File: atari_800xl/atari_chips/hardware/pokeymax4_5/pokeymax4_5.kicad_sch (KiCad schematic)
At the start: 0 parts

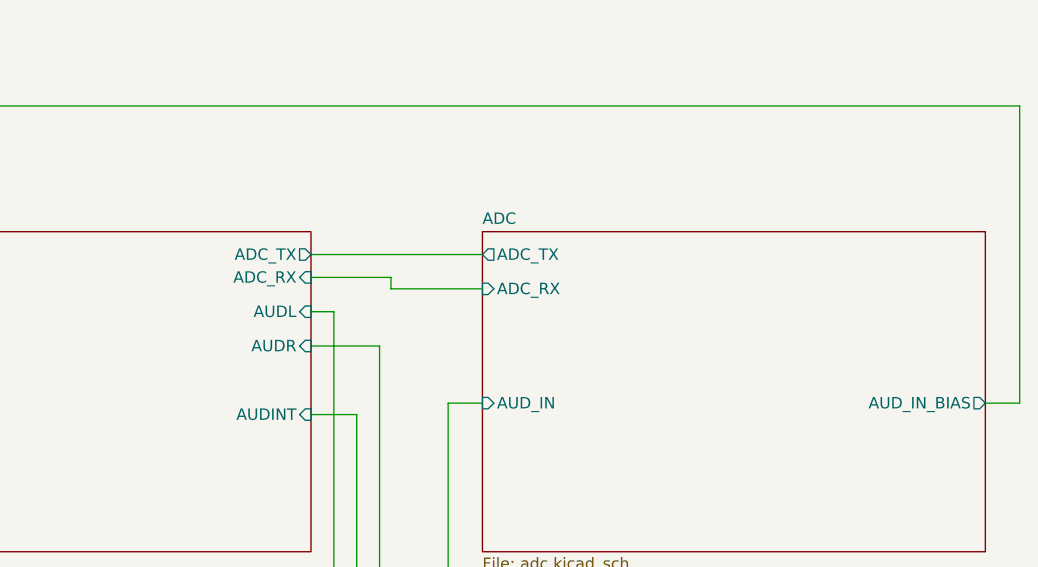
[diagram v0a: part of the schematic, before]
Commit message: Pokeymax v4_53 as produced
git-svn-id: svn+ssh://192.168.0.3/home/svnfpga/repo/trunk@1512 d6161ac3-aae1-4d52-9b05-ea9ac36b53d3
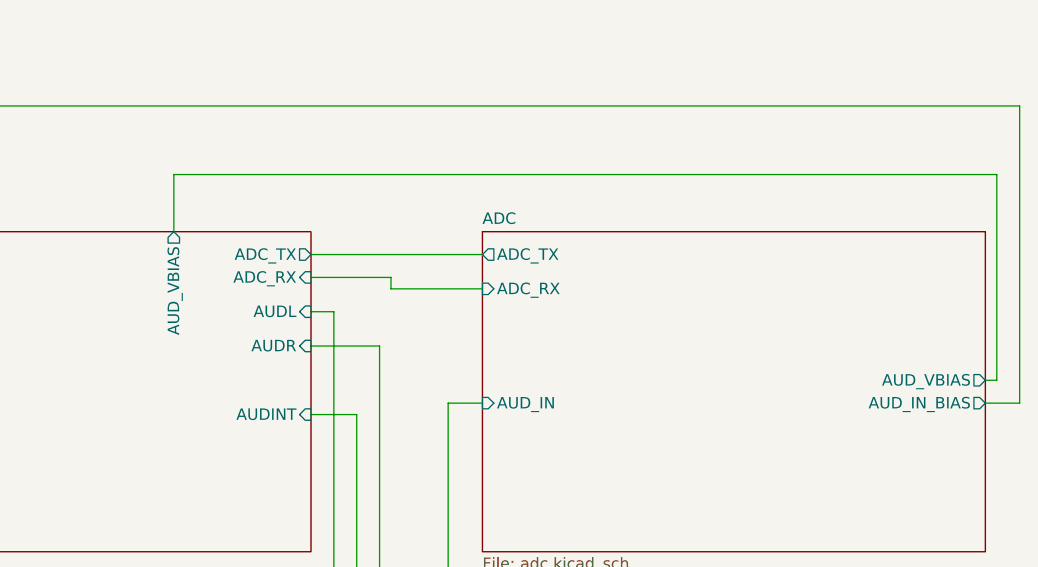
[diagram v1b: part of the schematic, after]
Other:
- sheet ADC ports: added AUD_VBIAS; removed none
- sheet FPGA ports: added AUD_VBIAS; removed none
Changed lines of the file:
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@@
+	(wire
+		(pts
+			(xy 251.46 68.58) (xy 160.02 68.58)
+		)
+		(stroke
+			(width 0)
+			(type default)
+		)
+	)
 	(wire
 		(pts
@@
 		)
 	)
+	(wire
+		(pts
+			(xy 250.19 91.44) (xy 251.46 91.44)
+		)
+		(stroke
+			(width 0)
+			(type default)
+		)
+	)
 	(bus
 		(pts
@@
 		(pts
 			(xy 113.03 147.32) (xy 113.03 148.59)
+		)
+		(stroke
+			(width 0)
+			(type default)
+		)
+	)
+	(wire
+		(pts
+			(xy 251.46 91.44) (xy 251.46 68.58)
+		)
+		(stroke
+			(width 0)
+			(type default)
+		)
+	)
+	(wire
+		(pts
+			(xy 160.02 68.58) (xy 160.02 74.93)
 		)
 		(stroke
@@
 			)
 		)
+		(pin "AUD_VBIAS" output
+			(at 250.19 91.44 0)
+			(effects
+				(font
+					(size 1.27 1.27)
+				)
+				(justify right)
+			)
+		)
 		(instances
 			(project "pokeymax4_5"
@@
 			(effects
 				(font
+					(size 1.27 1.27)
+				)
+				(justify right)
+			)
+		)
+		(pin "AUD_VBIAS" output
+			(at 160.02 74.93 90)
+			(effects
+				(font
